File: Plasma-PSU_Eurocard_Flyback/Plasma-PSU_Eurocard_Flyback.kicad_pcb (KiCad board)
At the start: 2 copper layers, 160 x 100 mm, 27 parts, among them J1 Molex Mini-fit Jr. 39-28-1243, J2 Molex Mini-fit Jr. 39-28-1083, J3 Molex Mini-fit Jr. 39-28-1083, J4 Pinheader Controls, J6 PWM_CN, K1 FINDER-40.52, Q1 BT169B, Q2 BT169B, Q3 TIP41C, Q4 TIP42C, Q5 IPW60, U1 RD_DPS5015, U2 Boost_48V_20A

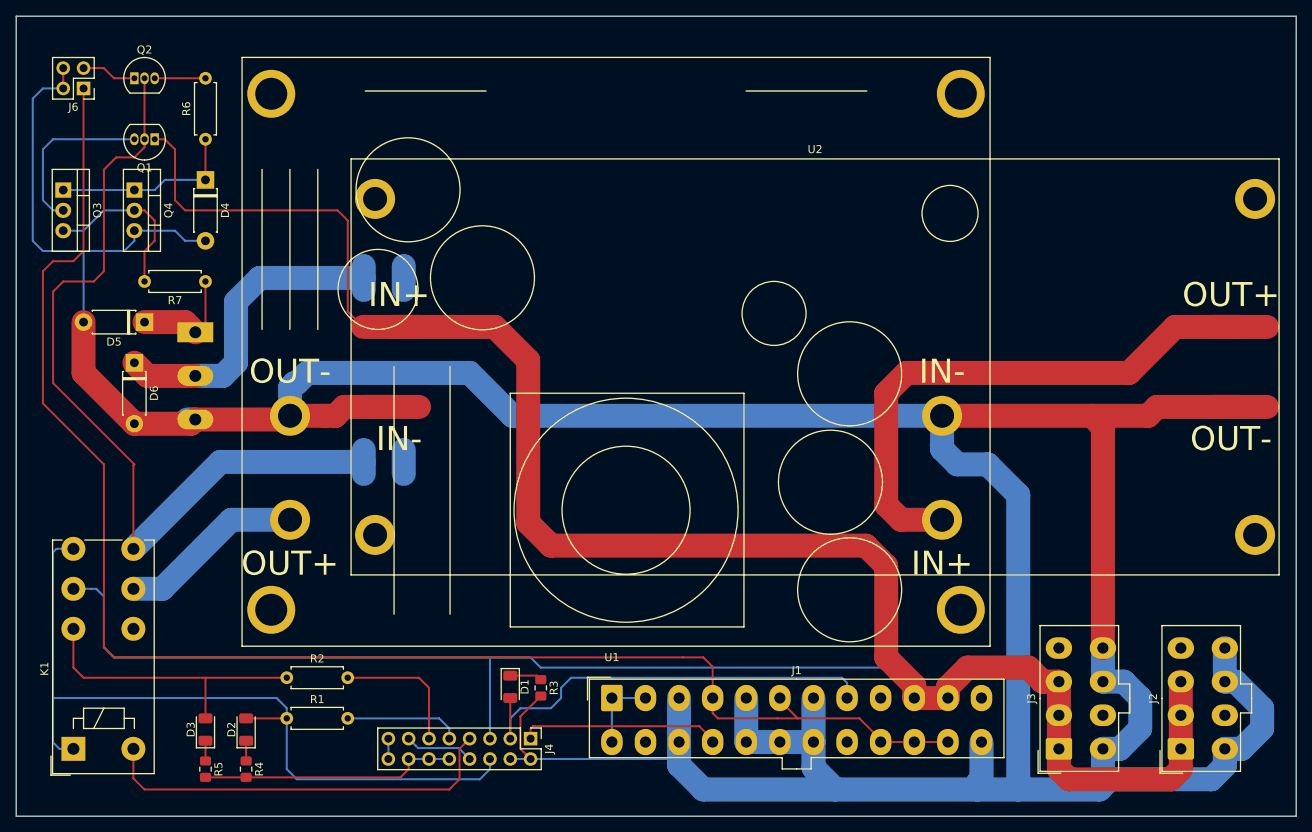
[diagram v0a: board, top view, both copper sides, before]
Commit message: LTC3786 arranged according to datasheet
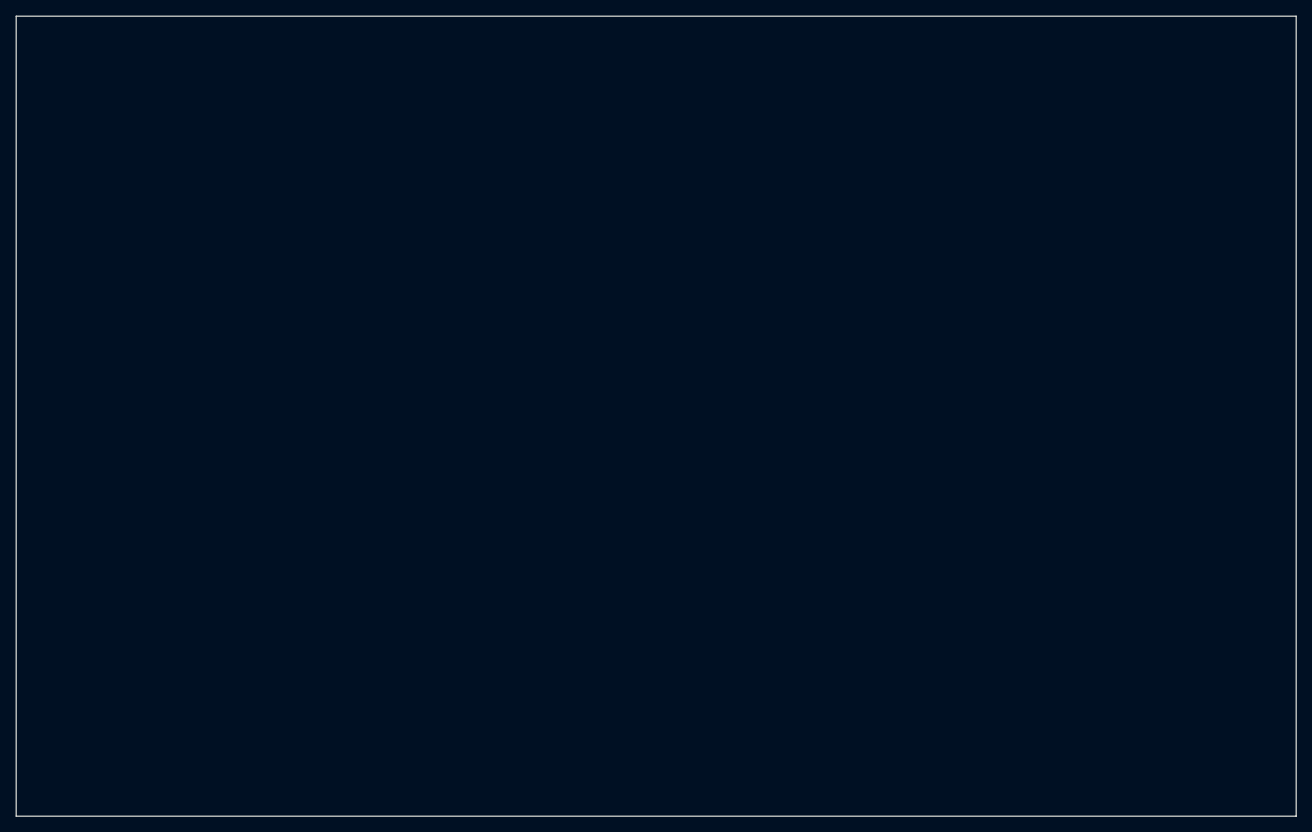
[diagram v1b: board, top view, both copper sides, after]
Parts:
- removed D1, D2, D3: LED, LED_SMD:LED_1206_3216Metric
- removed D4: ZD5, Diode_THT:D_DO-41_SOD81_P7.62mm_Horizontal
- removed D5: ZD20, Diode_THT:D_DO-41_SOD81_P7.62mm_Horizontal
- removed D6: UF4007, Diode_THT:D_DO-41_SOD81_P7.62mm_Horizontal
- removed J1: Molex Mini-fit Jr. 39-28-1243, Connector_Molex:Molex_Mini-Fit_Jr_5566-24A_2x12_P4.20mm_Vertical
- removed J2, J3: Molex Mini-fit Jr. 39-28-1083, Connector_Molex:Molex_Mini-Fit_Jr_5566-08A_2x04_P4.20mm_Vertical
- removed J4: Pinheader Controls, Connector_PinHeader_2.54mm:PinHeader_2x08_P2.54mm_Vertical
- removed J6: PWM_CN, Connector_PinHeader_2.54mm:PinHeader_2x02_P2.54mm_Vertical
- removed K1: FINDER-40.52, Relay_THT:Relay_DPDT_Finder_40.52
- removed L1: HV_Transformer, Plasma-PSU_Eurocard_Flyback:HF-HV_Transformer_15kV_300W
- removed Q1, Q2: BT169B, Package_TO_SOT_THT:TO-92_Inline
- removed Q3: TIP41C, Package_TO_SOT_THT:TO-220-3_Vertical
- removed Q4: TIP42C, Package_TO_SOT_THT:TO-220-3_Vertical
- removed Q5: IPW60, Package_TO_SOT_THT:TO-247-3_Vertical
- removed R1, R2: 180R, Resistor_THT:R_Axial_DIN0207_L6.3mm_D2.5mm_P7.62mm_Horizontal
- removed R3: 150R, Resistor_SMD:R_0805_2012Metric_Pad1.15x1.40mm_HandSolder
- removed R4, R5: 500R, Resistor_SMD:R_0805_2012Metric_Pad1.15x1.40mm_HandSolder
- removed R6: 300R, Resistor_THT:R_Axial_DIN0207_L6.3mm_D2.5mm_P7.62mm_Horizontal
- removed R7: 4R7, Resistor_THT:R_Axial_DIN0207_L6.3mm_D2.5mm_P7.62mm_Horizontal
- removed U1: RD_DPS5015, Plasma-PSU_Eurocard_Flyback:RD_DPS5015
- removed U2: Boost_48V_20A, Plasma-PSU_Eurocard_Flyback:Step_up_1200W_20A
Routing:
- net GND: track 534.1 -> 0.00 mm
- net +12V: track 338.9 -> 0.00 mm
- net +5V: track 194.1 -> 0.00 mm
- net Net-(K1-Pad24): track 104.7 -> 0.00 mm
- net PLASMA_ON_LED: track 99.5 -> 0.00 mm
- net +48V: track 69.3 -> 0.00 mm
- net PWR_GOOD: track 54.7 -> 0.00 mm
- net !PLASMA_STOP_BTN: track 51.2 -> 0.00 mm
- net Net-(D6-Pad1): track 38.9 -> 0.00 mm
- net PLASMA_OFF_LED: track 37.1 -> 0.00 mm
- net PWR_ON: track 25.1 -> 0.00 mm
- net Net-(D4-Pad1): track 23.4 -> 0.00 mm
- net +VSW: track 23.2 -> 0.00 mm
- net Net-(Q1-Pad3): track 21.4 -> 0.00 mm
- net Net-(Q3-Pad3): track 21.2 -> 0.00 mm
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
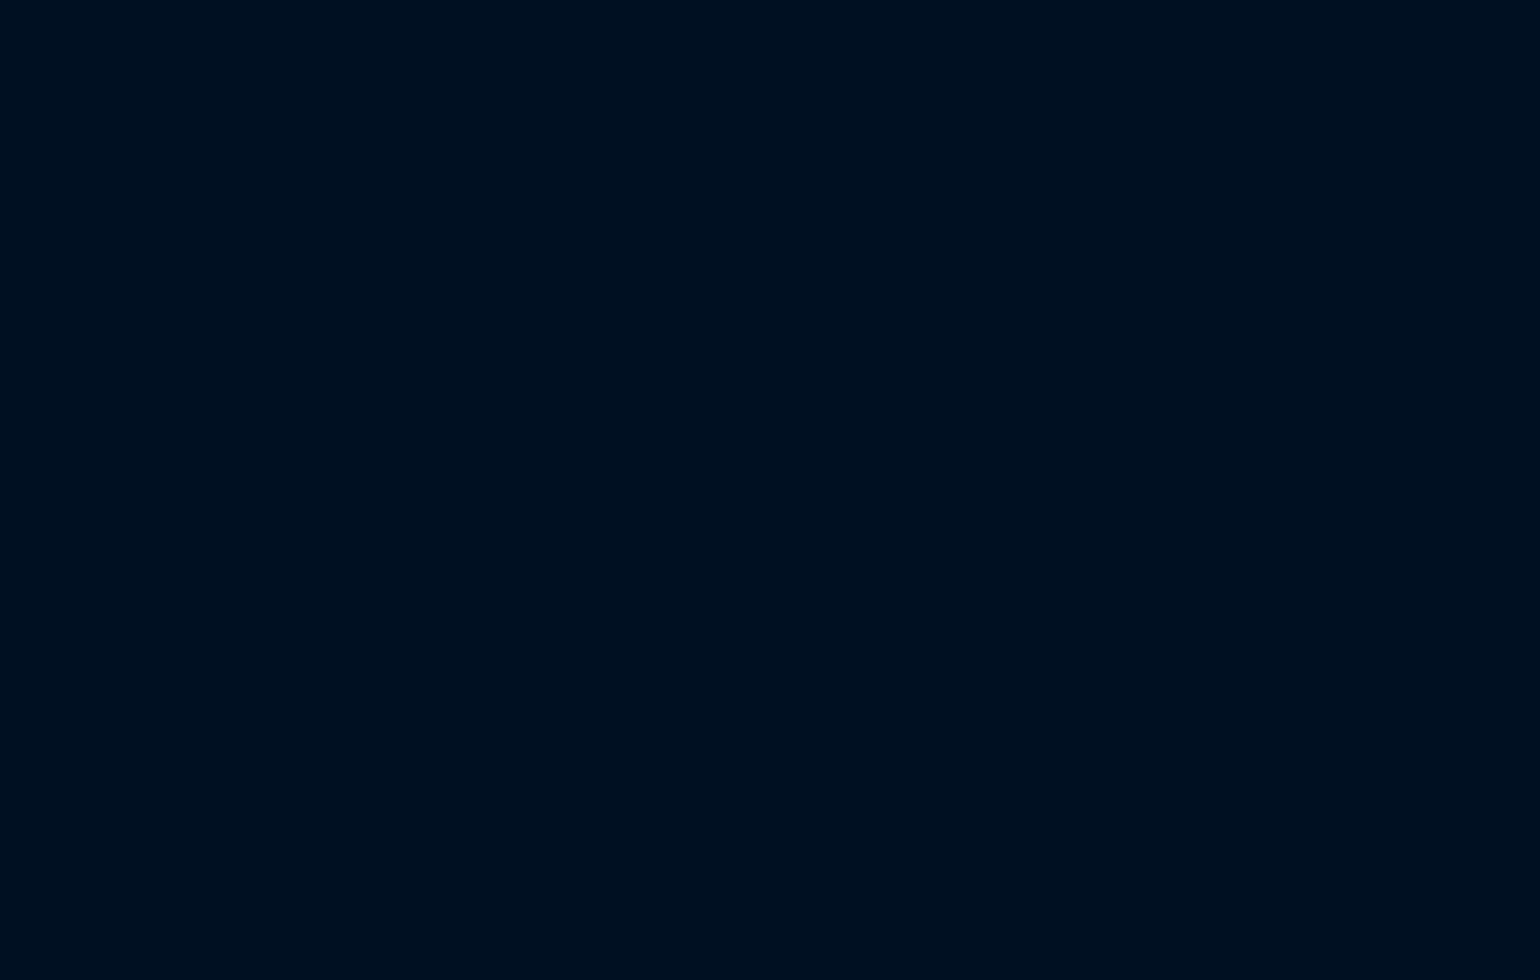
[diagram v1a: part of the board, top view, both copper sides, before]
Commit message: Footprints added
All footprints included, except:
- Boost Inductor
- 60A fuse holder
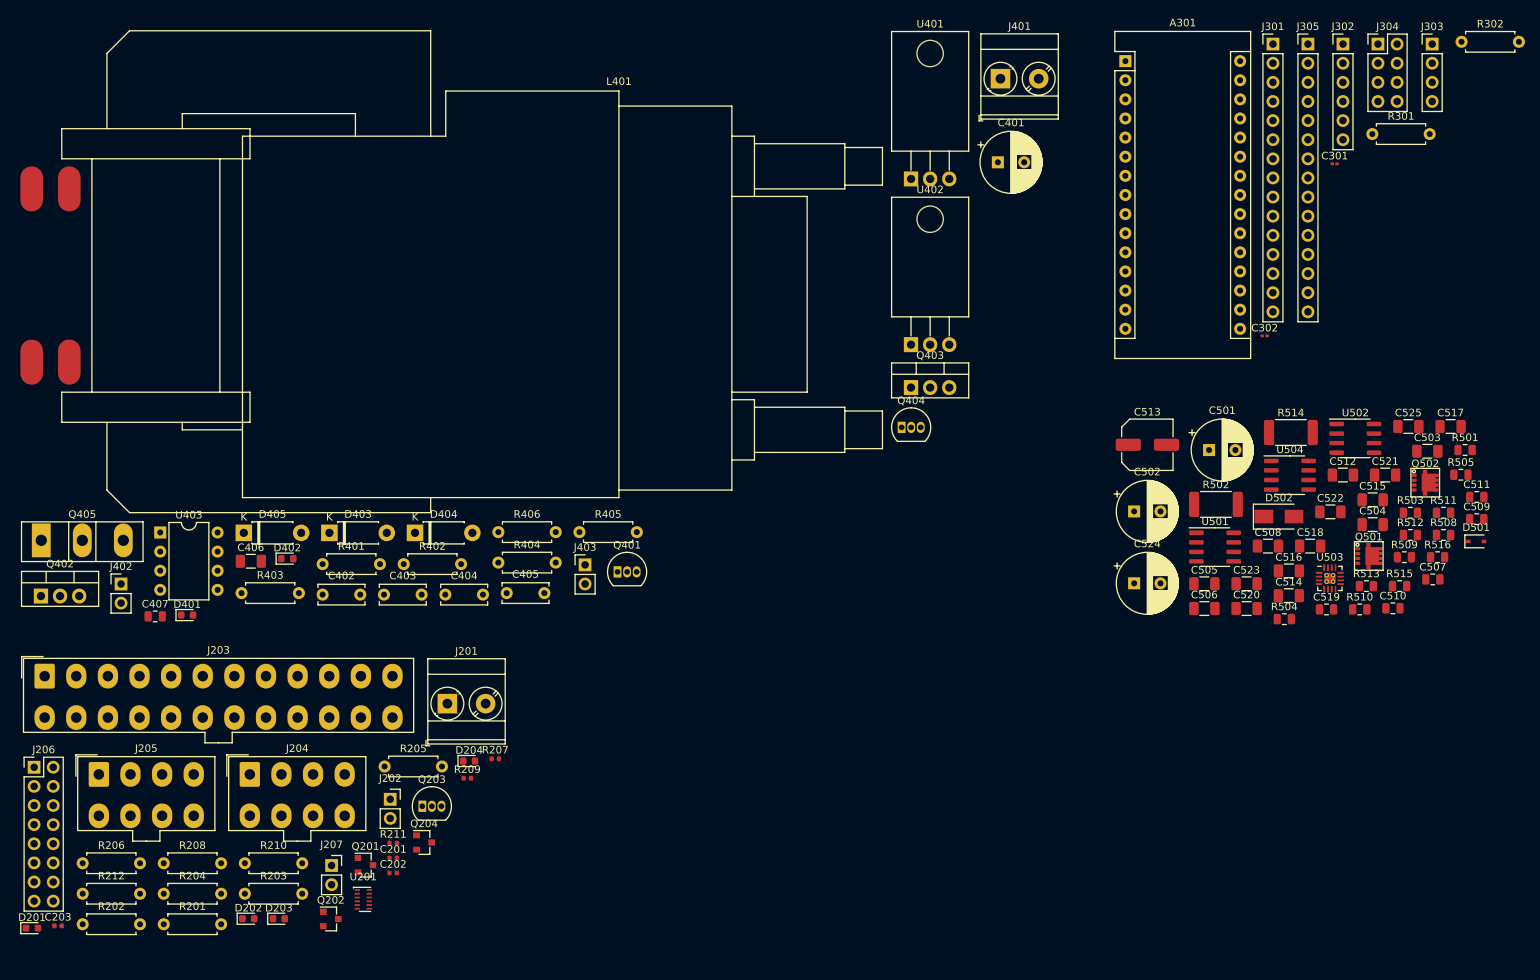
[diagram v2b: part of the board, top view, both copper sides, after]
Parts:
- added A301: Arduino_Nano_v3.x, Module:Arduino_Nano, F.Cu at (197.6, -150.9)
- added C201: 1µF, Capacitor_SMD:C_0402_1005Metric, F.Cu at (100.3, -45.0)
- added C202: 100nF, Capacitor_SMD:C_0402_1005Metric, F.Cu at (100.3, -43.0)
- added C203: 1µF, Capacitor_SMD:C_0402_1005Metric, F.Cu at (55.8, -36.0)
- added C301: 100n, Capacitor_SMD:C_0201_0603Metric, F.Cu at (225.4, -137.2)
- added C302: 100n, Capacitor_SMD:C_0201_0603Metric, F.Cu at (216.1, -114.4)
- added C401: 220µF, Capacitor_THT:CP_Radial_D8.0mm_P3.50mm, F.Cu at (180.6, -137.4)
- added C402: 6.8µF, Capacitor_THT:C_Disc_D6.0mm_W2.5mm_P5.00mm, F.Cu at (90.9, -80.0)
- added C403: 6.8µF, Capacitor_THT:C_Disc_D6.0mm_W2.5mm_P5.00mm, F.Cu at (99.1, -80.0)
- added C404: 6.8µF, Capacitor_THT:C_Disc_D6.0mm_W2.5mm_P5.00mm, F.Cu at (107.2, -80.0)
- added C405: 6.8µF, Capacitor_THT:C_Disc_D6.0mm_W2.5mm_P5.00mm, F.Cu at (115.4, -80.2)
- added C406: 100nF, Capacitor_SMD:C_1206_3216Metric, F.Cu at (81.4, -84.4)
- added C407: 10nF, Capacitor_SMD:C_0805_2012Metric, F.Cu at (68.7, -77.1)
- added C501: 220uF, Capacitor_THT:CP_Radial_D8.0mm_P3.50mm, F.Cu at (208.7, -99.2)
- added C502: 220uF, Capacitor_THT:CP_Radial_D8.0mm_P3.50mm, F.Cu at (198.7, -91.0)
- added C503: 6.8µF, Capacitor_SMD:C_1206_3216Metric, F.Cu at (237.7, -99.0)
- added C504: 6.8µF, Capacitor_SMD:C_1206_3216Metric, F.Cu at (230.4, -89.3)
- added C505: 100nF, Capacitor_SMD:C_1206_3216Metric, F.Cu at (208.1, -81.4)
- added C506: 100nF, Capacitor_SMD:C_1206_3216Metric, F.Cu at (208.1, -78.1)
- added C507: 10nF, Capacitor_SMD:C_0805_2012Metric, F.Cu at (238.4, -82.0)
- added C508: 100nF, Capacitor_SMD:C_1206_3216Metric, F.Cu at (216.5, -86.4)
- added C509: 10nF, Capacitor_SMD:C_0805_2012Metric, F.Cu at (244.2, -90.0)
- added C510: 15nF, Capacitor_SMD:C_0805_2012Metric, F.Cu at (233.1, -78.2)
- added C511: 220pF, Capacitor_SMD:C_0805_2012Metric, F.Cu at (244.2, -93.0)
- added C512: 100nF, Capacitor_SMD:C_1206_3216Metric, F.Cu at (226.5, -95.9)
- added C513: 10µF, Capacitor_SMD:C_Elec_6.3x5.8, F.Cu at (200.5, -99.9)
- added C514: 100nF, Capacitor_SMD:C_1206_3216Metric, F.Cu at (219.3, -79.9)
- added C515: 100nF, Capacitor_SMD:C_1206_3216Metric, F.Cu at (230.4, -92.6)
- added C516: 100nF, Capacitor_SMD:C_1206_3216Metric, F.Cu at (219.3, -83.1)
- added C517: 4.7µ MLCC, Capacitor_SMD:C_1206_3216Metric, F.Cu at (240.8, -102.3)
- added C518: 100nF, Capacitor_SMD:C_1206_3216Metric, F.Cu at (222.1, -86.4)
- added C519: 10nF, Capacitor_SMD:C_0805_2012Metric, F.Cu at (224.3, -78.0)
- added C520: 100nF, Capacitor_SMD:C_1206_3216Metric, F.Cu at (213.7, -78.1)
- added C521: 6.8µF, Capacitor_SMD:C_1206_3216Metric, F.Cu at (232.1, -95.9)
- added C522: 6.8µF, Capacitor_SMD:C_1206_3216Metric, F.Cu at (224.8, -91.0)
- added C523: 6.8µF, Capacitor_SMD:C_1206_3216Metric, F.Cu at (213.7, -81.4)
- added C524: 220uF, Capacitor_THT:CP_Radial_D8.0mm_P3.50mm, F.Cu at (198.7, -81.5)
- added C525: 100nF, Capacitor_SMD:C_1206_3216Metric, F.Cu at (235.1, -102.3)
- added D201: LED, LED_SMD:LED_0603_1608Metric, F.Cu at (52.3, -35.7)
- added D202: LED, LED_SMD:LED_0603_1608Metric, F.Cu at (81.1, -36.9)
- added D203: LED, LED_SMD:LED_0603_1608Metric, F.Cu at (85.1, -36.9)
- added D204: LED, LED_SMD:LED_0603_1608Metric, F.Cu at (110.4, -57.9)
- added D401: PWM_LED, LED_SMD:LED_0603_1608Metric, F.Cu at (73.0, -77.3)
- added D402: ENBL_LED, LED_SMD:LED_0603_1608Metric, F.Cu at (86.3, -84.8)
- added D403: ZD5, Diode_THT:D_DO-41_SOD81_P7.62mm_Horizontal, F.Cu at (91.8, -88.2)
- added D404: ZD20, Diode_THT:D_DO-41_SOD81_P7.62mm_Horizontal, F.Cu at (103.2, -88.2)
- added D405: UF4007, Diode_THT:D_DO-41_SOD81_P7.62mm_Horizontal, F.Cu at (80.5, -88.2)
- added D501: ZD5, Diode_SMD:D_SOD-323, F.Cu at (244.2, -87.1)
- added D502: B120-E3, Diode_SMD:D_SMA, F.Cu at (218.0, -90.4)
- added J201: PWR_FWD, TerminalBlock_Phoenix:TerminalBlock_Phoenix_MKDS-3-2-5.08_1x02_P5.08mm_Horizontal, F.Cu at (107.5, -65.5)
- added J202: PWM_FWD, Connector_PinSocket_2.54mm:PinSocket_1x02_P2.54mm_Vertical, F.Cu at (99.9, -52.8)
- added J203: Molex Mini-fit Jr. 39-28-1243, Connector_Molex:Molex_Mini-Fit_Jr_5566-24A_2x12_P4.20mm_Vertical, F.Cu at (54.0, -69.2)
- added J204: Molex Mini-fit Jr. 39-28-1083, Connector_Molex:Molex_Mini-Fit_Jr_5566-08A_2x04_P4.20mm_Vertical, F.Cu at (81.3, -56.1)
- added J205: Molex Mini-fit Jr. 39-28-1083, Connector_Molex:Molex_Mini-Fit_Jr_5566-08A_2x04_P4.20mm_Vertical, F.Cu at (61.2, -56.1)
- added J206: Pinheader Controls, Connector_PinHeader_2.54mm:PinHeader_2x08_P2.54mm_Vertical, F.Cu at (52.6, -57.1)
- added J207: ENBL_FWD, Connector_PinSocket_2.54mm:PinSocket_1x02_P2.54mm_Vertical, F.Cu at (92.1, -44.0)
- added J301: Arduino_Pinout_01-15, Connector_PinHeader_2.54mm:PinHeader_1x15_P2.54mm_Vertical, F.Cu at (217.2, -153.1)
- added J302: SPI, Connector_PinHeader_2.54mm:PinHeader_1x06_P2.54mm_Vertical, F.Cu at (226.5, -153.1)
- added J303: UART, Connector_PinHeader_2.54mm:PinHeader_1x04_P2.54mm_Vertical, F.Cu at (238.3, -153.1)
- added J304: I2C, Connector_PinHeader_2.54mm:PinHeader_2x04_P2.54mm_Vertical, F.Cu at (231.1, -153.1)
- added J305: Arduino_Pinout_16-30, Connector_PinHeader_2.54mm:PinHeader_1x15_P2.54mm_Vertical, F.Cu at (221.8, -153.1)
- added J401: PWR_IN, TerminalBlock_Phoenix:TerminalBlock_Phoenix_MKDS-3-2-5.08_1x02_P5.08mm_Horizontal, F.Cu at (181.0, -148.5)
- added J402: PWM_IN, Connector_PinHeader_2.54mm:PinHeader_1x02_P2.54mm_Vertical, F.Cu at (64.2, -81.4)
- added J403: ENBL_IN, Connector_PinHeader_2.54mm:PinHeader_1x02_P2.54mm_Vertical, F.Cu at (125.8, -83.9)
- added L401: HV_Transformer, Plasma-PSU_Eurocard_Flyback:HF-HV_Transformer_15kV_300W, F.Cu at (130.3, -146.9)
- added Q201: BC818, Package_TO_SOT_SMD:SOT-23, F.Cu at (96.6, -44.1)
- added Q202: BC818, Package_TO_SOT_SMD:SOT-23, F.Cu at (92.0, -36.9)
- added Q203: BT169B, Package_TO_SOT_THT:TO-92_Inline, F.Cu at (104.2, -51.9)
- added Q204: BC808, Package_TO_SOT_SMD:SOT-23, F.Cu at (104.4, -47.1)
- added Q401: BT169B, Package_TO_SOT_THT:TO-92_Inline, F.Cu at (130.1, -83.0)
- added Q402: TIP41C, Package_TO_SOT_THT:TO-220-3_Vertical, F.Cu at (53.5, -79.8)
- added Q403: TIP42C, Package_TO_SOT_THT:TO-220-3_Vertical, F.Cu at (169.1, -107.5)
- added Q404: BT169B, Package_TO_SOT_THT:TO-92_Inline, F.Cu at (167.8, -102.2)
- added Q405: IPW60, Package_TO_SOT_THT:TO-247-3_Vertical, F.Cu at (53.6, -87.2)
- added Q501: NVTFS6H850NL, Plasma-PSU_Eurocard_Flyback:ONSEMI-µ8FL, F.Cu at (229.9, -85.1)
- added Q502: NVTFS6H850NL, Plasma-PSU_Eurocard_Flyback:ONSEMI-µ8FL, F.Cu at (237.4, -94.9)
- added R201: 10k, Resistor_THT:R_Axial_DIN0207_L6.3mm_D2.5mm_P7.62mm_Horizontal, F.Cu at (69.8, -36.2)
- added R202: 10k, Resistor_THT:R_Axial_DIN0207_L6.3mm_D2.5mm_P7.62mm_Horizontal, F.Cu at (59.1, -36.2)
- added R203: 10k, Resistor_THT:R_Axial_DIN0207_L6.3mm_D2.5mm_P7.62mm_Horizontal, F.Cu at (80.6, -40.3)
- added R204: 10k, Resistor_THT:R_Axial_DIN0207_L6.3mm_D2.5mm_P7.62mm_Horizontal, F.Cu at (69.8, -40.3)
- added R205: 470R, Resistor_THT:R_Axial_DIN0207_L6.3mm_D2.5mm_P7.62mm_Horizontal, F.Cu at (99.2, -57.2)
- added R206: 1k, Resistor_THT:R_Axial_DIN0207_L6.3mm_D2.5mm_P7.62mm_Horizontal, F.Cu at (59.1, -44.3)
- added R207: 470R, Resistor_SMD:R_0402_1005Metric, F.Cu at (113.9, -58.2)
- added R208: 1k, Resistor_THT:R_Axial_DIN0207_L6.3mm_D2.5mm_P7.62mm_Horizontal, F.Cu at (69.8, -44.3)
- added R209: 470R, Resistor_SMD:R_0402_1005Metric, F.Cu at (110.2, -55.6)
- added R210: 1k, Resistor_THT:R_Axial_DIN0207_L6.3mm_D2.5mm_P7.62mm_Horizontal, F.Cu at (80.6, -44.3)
- added R211: 470R, Resistor_SMD:R_0402_1005Metric, F.Cu at (100.3, -47.0)
- added R212: 1k, Resistor_THT:R_Axial_DIN0207_L6.3mm_D2.5mm_P7.62mm_Horizontal, F.Cu at (59.1, -40.3)
- added R301: 4.8k, Resistor_THT:R_Axial_DIN0207_L6.3mm_D2.5mm_P7.62mm_Horizontal, F.Cu at (230.4, -141.2)
- added R302: 4.8k, Resistor_THT:R_Axial_DIN0207_L6.3mm_D2.5mm_P7.62mm_Horizontal, F.Cu at (242.2, -153.4)
- added R401: 250R, Resistor_THT:R_Axial_DIN0207_L6.3mm_D2.5mm_P7.62mm_Horizontal, F.Cu at (90.9, -84.0)
- added R402: 250R, Resistor_THT:R_Axial_DIN0207_L6.3mm_D2.5mm_P7.62mm_Horizontal, F.Cu at (101.7, -84.0)
- added R403: 1k, Resistor_THT:R_Axial_DIN0207_L6.3mm_D2.5mm_P7.62mm_Horizontal, F.Cu at (80.2, -80.2)
- added R404: 1k, Resistor_THT:R_Axial_DIN0207_L6.3mm_D2.5mm_P7.62mm_Horizontal, F.Cu at (114.3, -84.2)
- added R405: 300R, Resistor_THT:R_Axial_DIN0207_L6.3mm_D2.5mm_P7.62mm_Horizontal, F.Cu at (125.1, -88.3)
- added R406: 4R7, Resistor_THT:R_Axial_DIN0207_L6.3mm_D2.5mm_P7.62mm_Horizontal, F.Cu at (114.3, -88.3)
- added R501: 8.66k, Resistor_SMD:R_0805_2012Metric, F.Cu at (242.7, -99.2)
- added R502: 2mR, Resistor_SMD:R_2512_6332Metric, F.Cu at (209.6, -92.0)
- added R503: 100k, Resistor_SMD:R_0805_2012Metric, F.Cu at (235.4, -90.9)
- added R504: 100k, Resistor_SMD:R_0805_2012Metric, F.Cu at (218.7, -76.7)
- added R505: 100k, Resistor_SMD:R_0805_2012Metric, F.Cu at (242.1, -95.9)
- added R508: 100k, Resistor_SMD:R_0805_2012Metric, F.Cu at (239.8, -87.9)
- added R509: 34k, Resistor_SMD:R_0805_2012Metric, F.Cu at (234.6, -85.0)
- added R510: 2k, Resistor_SMD:R_0805_2012Metric, F.Cu at (228.7, -78.0)
- added R511: 4.8k, Resistor_SMD:R_0805_2012Metric, F.Cu at (239.8, -90.9)
- added R512: 100k, Resistor_SMD:R_0805_2012Metric, F.Cu at (235.4, -87.9)
- added R513: 3.3k, Resistor_SMD:R_0805_2012Metric, F.Cu at (229.6, -81.1)
- added R514: 1mR (2512), Resistor_SMD:R_2512_6332Metric, F.Cu at (219.5, -101.5)
- added R515: 3.3k, Resistor_SMD:R_0805_2012Metric, F.Cu at (234.0, -81.1)
- added R516: 100k, Resistor_SMD:R_0805_2012Metric, F.Cu at (239.0, -85.0)
- added U201: STM6600, Package_DFN_QFN:TDFN-12_2x3mm_P0.5mm, F.Cu at (96.3, -39.5)
- added U401: L7812, Package_TO_SOT_THT:TO-220-3_Horizontal_TabDown, F.Cu at (169.1, -135.2)
- added U402: L7805, Package_TO_SOT_THT:TO-220-3_Horizontal_TabDown, F.Cu at (169.1, -113.2)
- added U403: ILD74, Package_DIP:DIP-8_W7.62mm, F.Cu at (69.4, -88.2)
- added U501: MCP602, Package_SO:SOIC-8_3.9x4.9mm_P1.27mm, F.Cu at (209.5, -86.3)
- added U502: MCP602, Package_SO:SOIC-8_3.9x4.9mm_P1.27mm, F.Cu at (228.1, -100.7)
- added U503: LTC3786, Package_DFN_QFN:QFN-16-1EP_3x3mm_P0.5mm_EP1.45x1.45mm_ThermalVias, F.Cu at (224.7, -82.1)
- added U504: MCP4822, Package_SO:SOIC-8_3.9x4.9mm_P1.27mm, F.Cu at (219.4, -95.9)
